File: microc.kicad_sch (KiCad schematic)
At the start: 11 parts, among them SW1 SW_SPST

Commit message: Cleaning up layout
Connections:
- net +3V3: now also C13.2, C14.2; no longer C13.1, C14.1
- net GND: now also C13.1, C14.1; no longer C13.2, C14.2
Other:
- moved on the sheet: C13, C14, LED1, MC1, NTC1, R19, R21, R23, R7, R8, SW1

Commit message: All parts on. Set foots for everything. Time to try a layout.
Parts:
- C13, C14: footprint (none) -> Capacitor_SMD:C_0402_1005Metric
- LED1: footprint (none) -> LED_THT:LED_D3.0mm-3
- NTC1, R21, R7, R8: footprint (none) -> Resistor_SMD:R_0402_1005Metric
- R19: footprint (none) -> Resistor_SMD:R_0603_1608Metric
- R23: value R_US -> 1KΩ; footprint (none) -> Resistor_SMD:R_0402_1005Metric
- SW1: footprint (none) -> Button_Switch_THT:SW_SPST_Omron_B3F-315x_Angled
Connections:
- net at LED1.1 (K1): now also R21.2; no longer R19.2
- net at LED1.3 (K2): now also R19.2; no longer R21.2
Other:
- note added: "pin 1 from edge 1 is red 3 is green"
- note removed: "pin 1 near edge 1 is green 3 is red"
- moved on the sheet: R19, R21, R8
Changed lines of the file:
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@@
 		)
 	)
-	(text "pin 1 near edge\n1 is green\n3 is red"
+	(text "pin 1 from edge\n1 is red\n3 is green\n"
 		(exclude_from_sim no)
 		(at 124.46 193.04 0)
@@
 	(wire
 		(pts
-			(xy 127 72.39) (xy 127 77.47)
+			(xy 127 72.39) (xy 127 74.93)
 		)
 		(stroke
@@
 	(wire
 		(pts
-			(xy 127 85.09) (xy 127 86.36)
+			(xy 127 82.55) (xy 127 86.36)
 		)
 		(stroke
@@
 	(global_label "~{LED_RED}"
 		(shape input)
-		(at 96.52 179.07 180)
+		(at 96.52 173.99 180)
 		(fields_autoplaced yes)
 		(effects
@@
 		)
 		(property "Intersheetrefs" "${INTERSHEET_REFS}"
-			(at 85.4311 179.07 0)
+			(at 85.4311 173.99 0)
 			(effects
 				(font
@@
 	(global_label "~{LED_GREEN}"
 		(shape input)
-		(at 96.52 173.99 180)
+		(at 96.52 179.07 180)
 		(fields_autoplaced yes)
 		(effects
@@
 		)
 		(property "Intersheetrefs" "${INTERSHEET_REFS}"
-			(at 82.9516 173.99 0)
+			(at 82.9516 179.07 0)
 			(effects
 				(font
@@
 	(symbol
 		(lib_id "Device:R_US")
-		(at 127 81.28 180)
+		(at 127 78.74 180)
 		(unit 1)
 		(exclude_from_sim no)
@@
 		(fields_autoplaced yes)
 		(property "Reference" "R8"
+			(at 129.54 77.4699 0)
+			(effects
+				(font
+					(size 1.27 1.27)
+				)
+				(justify right)
+			)
+		)
+		(property "Value" "R_US"
 			(at 129.54 80.0099 0)
 			(effects
@@
 			)
 		)
-		(property "Value" "R_US"
-			(at 129.54 82.5499 0)
-			(effects
-				(font
-					(size 1.27 1.27)
-				)
-				(justify right)
-			)
-		)
-		(property "Footprint" ""
-			(at 125.984 81.026 90)
+		(property "Footprint" "Resistor_SMD:R_0402_1005Metric"
+			(at 125.984 78.486 90)
 			(effects
 				(font
@@
 		)
 		(property "Datasheet" "~"
-			(at 127 81.28 0)
+			(at 127 78.74 0)
 			(effects
 				(font
@@
 		)
 		(property "Description" "Resistor, US symbol"
-			(at 127 81.28 0)
+			(at 127 78.74 0)
 			(effects
 				(font
@@
 			)
 		)
-		(property "Footprint" ""
+		(property "Footprint" "Capacitor_SMD:C_0402_1005Metric"
 			(at 113.9952 55.88 0)
 			(effects
@@
 		(fields_autoplaced yes)
 		(property "Reference" "R23"
-			(at 83.82 57.1501 0)
+			(at 83.82 54.6099 0)
 			(effects
 				(font
@@
 			)
 		)
-		(property "Value" "R_US"
-			(at 83.82 54.6101 0)
+		(property "Value" "1KΩ"
+			(at 83.82 57.1499 0)
 			(effects
 				(font
@@
 			)
 		)
-		(property "Footprint" ""
+		(property "Footprint" "Resistor_SMD:R_0402_1005Metric"
 			(at 80.264 56.134 90)
 			(effects
@@
 			)
 		)
-		(property "Footprint" ""
+		(property "Footprint" "LED_THT:LED_D3.0mm-3"
 			(at 124.46 176.53 0)
 			(effects
@@
 	(symbol
 		(lib_id "Device:R_US")
-		(at 107.95 179.07 90)
+		(at 107.95 173.99 90)
 		(unit 1)
 		(exclude_from_sim no)
@@
 		(fields_autoplaced yes)
 		(property "Reference" "R21"
-			(at 107.95 182.88 90)
+			(at 107.95 167.64 90)
 			(effects
 				(font
@@
 		)
 		(property "Value" "1kΩ"
-			(at 107.95 185.42 90)
-			(effects
-				(font
-					(size 1.27 1.27)
-				)
-			)
-		)
-		(property "Footprint" ""
-			(at 108.204 178.054 90)
+			(at 107.95 170.18 90)
+			(effects
+				(font
+					(size 1.27 1.27)
+				)
+			)
+		)
+		(property "Footprint" "Resistor_SMD:R_0402_1005Metric"
+			(at 108.204 172.974 90)
 			(effects
 				(font
@@
 		)
 		(property "Datasheet" "~"
-			(at 107.95 179.07 0)
+			(at 107.95 173.99 0)
 			(effects
 				(font
@@
 		)
 		(property "Description" "Resistor, US symbol"
-			(at 107.95 179.07 0)
+			(at 107.95 173.99 0)
 			(effects
 				(font
@@
 			)
 		)
-		(property "Footprint" ""
+		(property "Footprint" "Capacitor_SMD:C_0402_1005Metric"
 			(at 101.2952 55.88 0)
 			(effects
@@
 			)
 		)
-		(property "Footprint" ""
+		(property "Footprint" "Resistor_SMD:R_0402_1005Metric"
 			(at 118.364 73.406 90)
 			(effects
@@
 		(fields_autoplaced yes)
 		(property "Reference" "SW1"
-			(at 60.96 66.04 0)
+			(at 60.96 54.61 0)
 			(effects
 				(font
@@
 		)
 		(property "Value" "SW_SPST"
-			(at 60.96 63.5 0)
-			(effects
-				(font
-					(size 1.27 1.27)
-				)
-			)
-		)
-		(property "Footprint" ""
+			(at 60.96 57.15 0)
+			(effects
+				(font
+					(size 1.27 1.27)
+				)
+			)
+		)
+		(property "Footprint" "Button_Switch_THT:SW_SPST_Omron_B3F-315x_Angled"
 			(at 60.96 59.69 0)
 			(effects
@@
 			)
 		)
-		(property "Footprint" ""
+		(property "Footprint" "Resistor_SMD:R_0402_1005Metric"
 			(at 127 64.77 0)
 			(effects
@@
 	(symbol
 		(lib_id "Device:R_US")
-		(at 107.95 173.99 90)
+		(at 107.95 179.07 90)
 		(unit 1)
 		(exclude_from_sim no)
@@
 		(fields_autoplaced yes)
 		(property "Reference" "R19"
-			(at 107.95 167.64 90)
+			(at 107.95 182.88 90)
 			(effects
 				(font
@@
 		)
 		(property "Value" "10kΩ"
-			(at 107.95 170.18 90)
-			(effects
-				(font
-					(size 1.27 1.27)
-				)
-			)
-		)
-		(property "Footprint" ""
-			(at 108.204 172.974 90)
+			(at 107.95 185.42 90)
+			(effects
+				(font
+					(size 1.27 1.27)
+				)
+			)
+		)
+		(property "Footprint" "Resistor_SMD:R_0603_1608Metric"
+			(at 108.204 178.054 90)
 			(effects
 				(font
@@
 		)
 		(property "Datasheet" "~"
-			(at 107.95 173.99 0)
+			(at 107.95 179.07 0)
 			(effects
 				(font
@@
 		)
 		(property "Description" "Resistor, US symbol"
-			(at 107.95 173.99 0)
-			(effects
-				(font
+			(at 107.95 179.07 0)
+			(effects
+				(font

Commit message: Made a first board layout.
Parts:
- R19: footprint Resistor_SMD:R_0603_1608Metric -> Resistor_SMD:R_0402_1005Metric
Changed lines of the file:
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@@
 			)
 		)
-		(property "Footprint" "Resistor_SMD:R_0603_1608Metric"
+		(property "Footprint" "Resistor_SMD:R_0402_1005Metric"
 			(at 108.204 178.054 90)
 			(effects

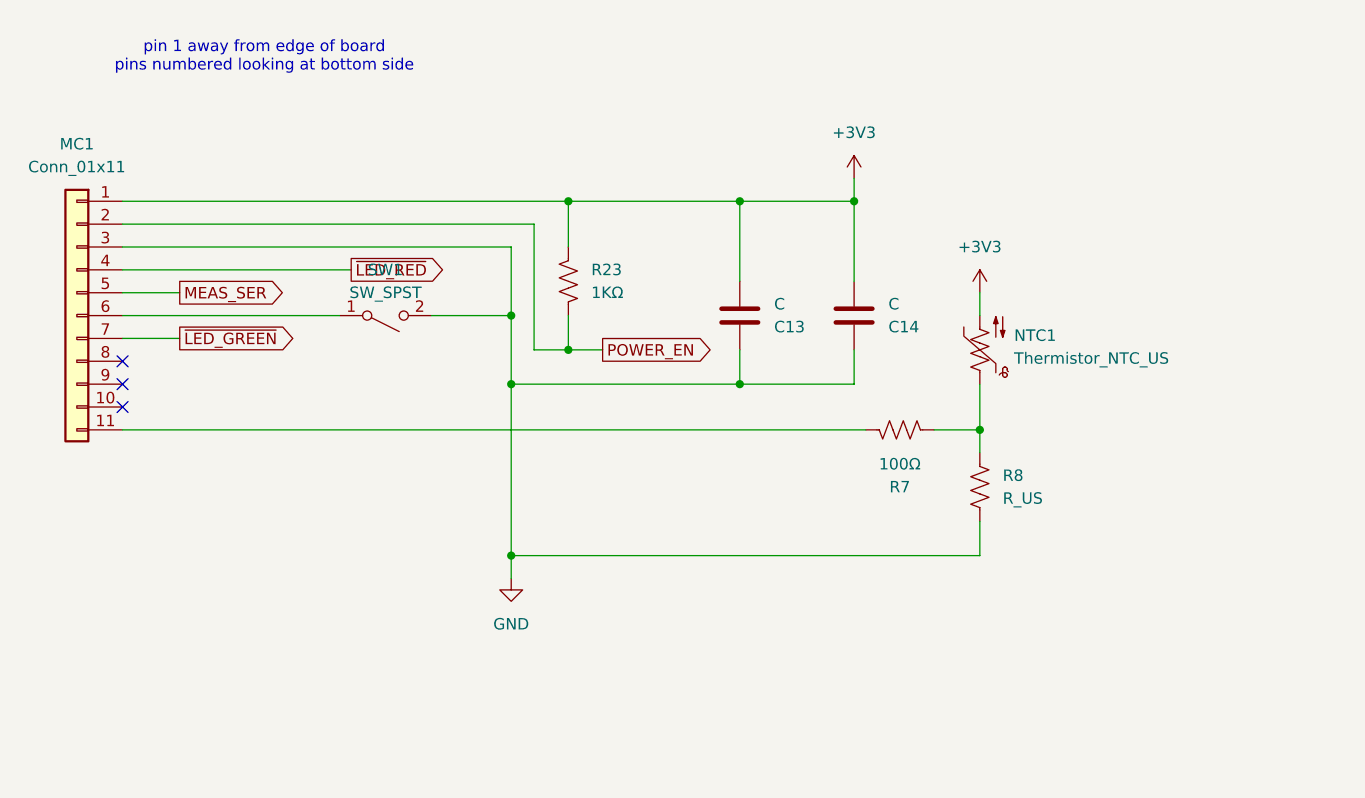
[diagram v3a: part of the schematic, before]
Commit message: Have a full board layout which resembles the original in some ways. Made a few schematic fixes to match better.
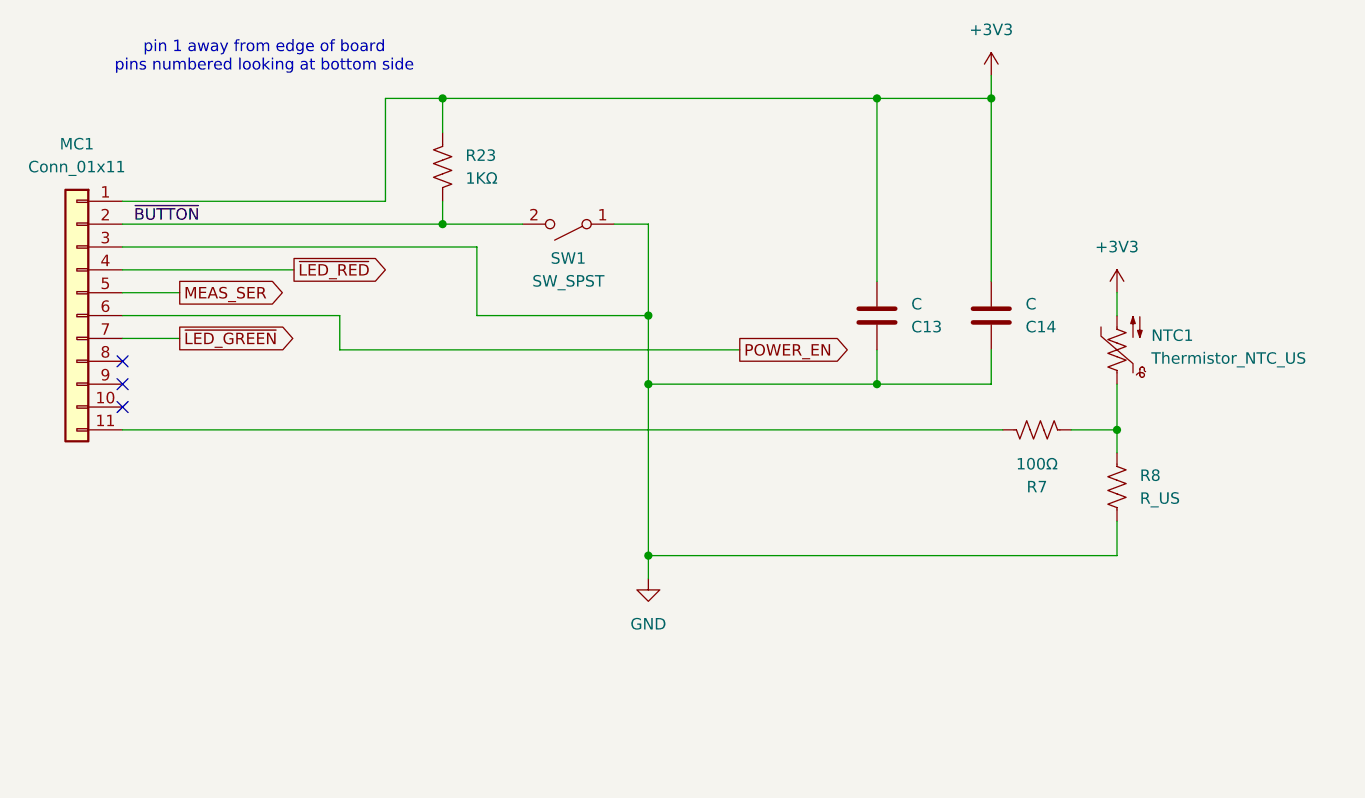
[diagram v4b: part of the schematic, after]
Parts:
- MC1: footprint Connector_PinHeader_1.00mm:PinHeader_1x11_P1.00mm_Vertical_SMD_Pin1Left -> HF relays:BoardToBoardInterface_11xP1.00mm
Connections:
- net GND: now also SW1.1 (A); no longer SW1.2 (B)
- net POWER_EN: now also MC1.6 (Pin_6); no longer MC1.2 (Pin_2), R23.2
- new net ~{BUTTON}: MC1.2 (Pin_2), R23.2, SW1.2 (B)
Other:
- moved on the sheet: C13, C14, NTC1, R23, R7, R8, SW1
